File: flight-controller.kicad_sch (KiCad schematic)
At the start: 83 parts, among them J1 USB_C_Receptacle_USB2.0, J2 ESC, J3 RX, J4 GPS, J5 I2C, J6 Camera, J7 VTX, J8 DVTX, Q1 AO3400A, SW1 SW_Push, U1 AT32F435RGT7, U2 BMI270, U3 BMP280, U4 W25N01GVZEIG, U5 AT7456E, U6 TPS54302, U7 TPS54302, U8 TLV75733PDBV, U9 USBLC6-2P6, Y1 27MHz, Y2 8MHz

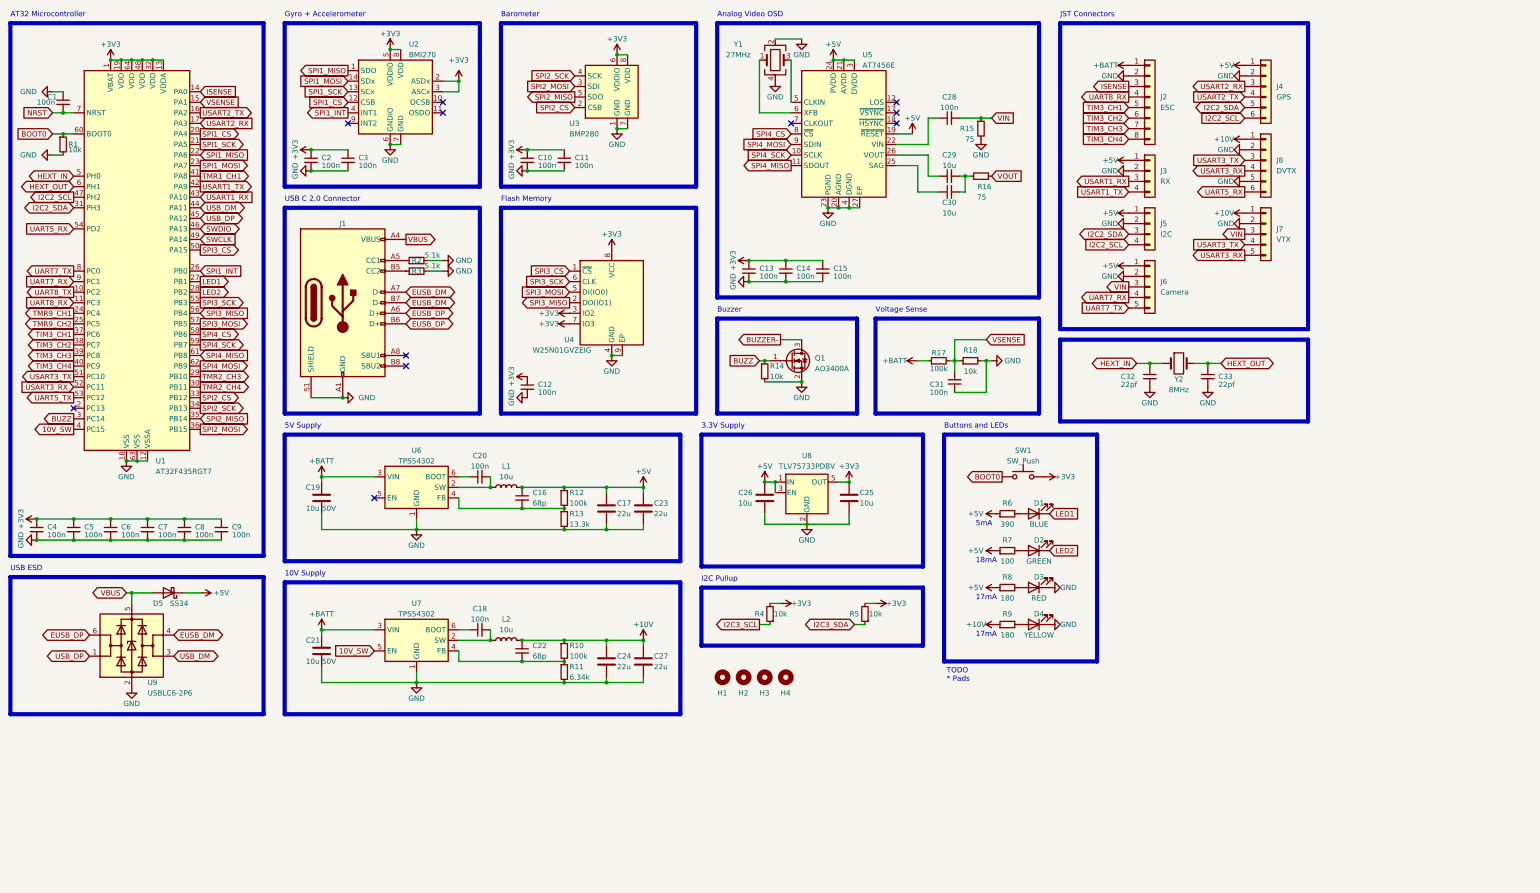
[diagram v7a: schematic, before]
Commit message: Change LED resistors to reduce current, tidy up schematic sheet, changes to AT32 pinout
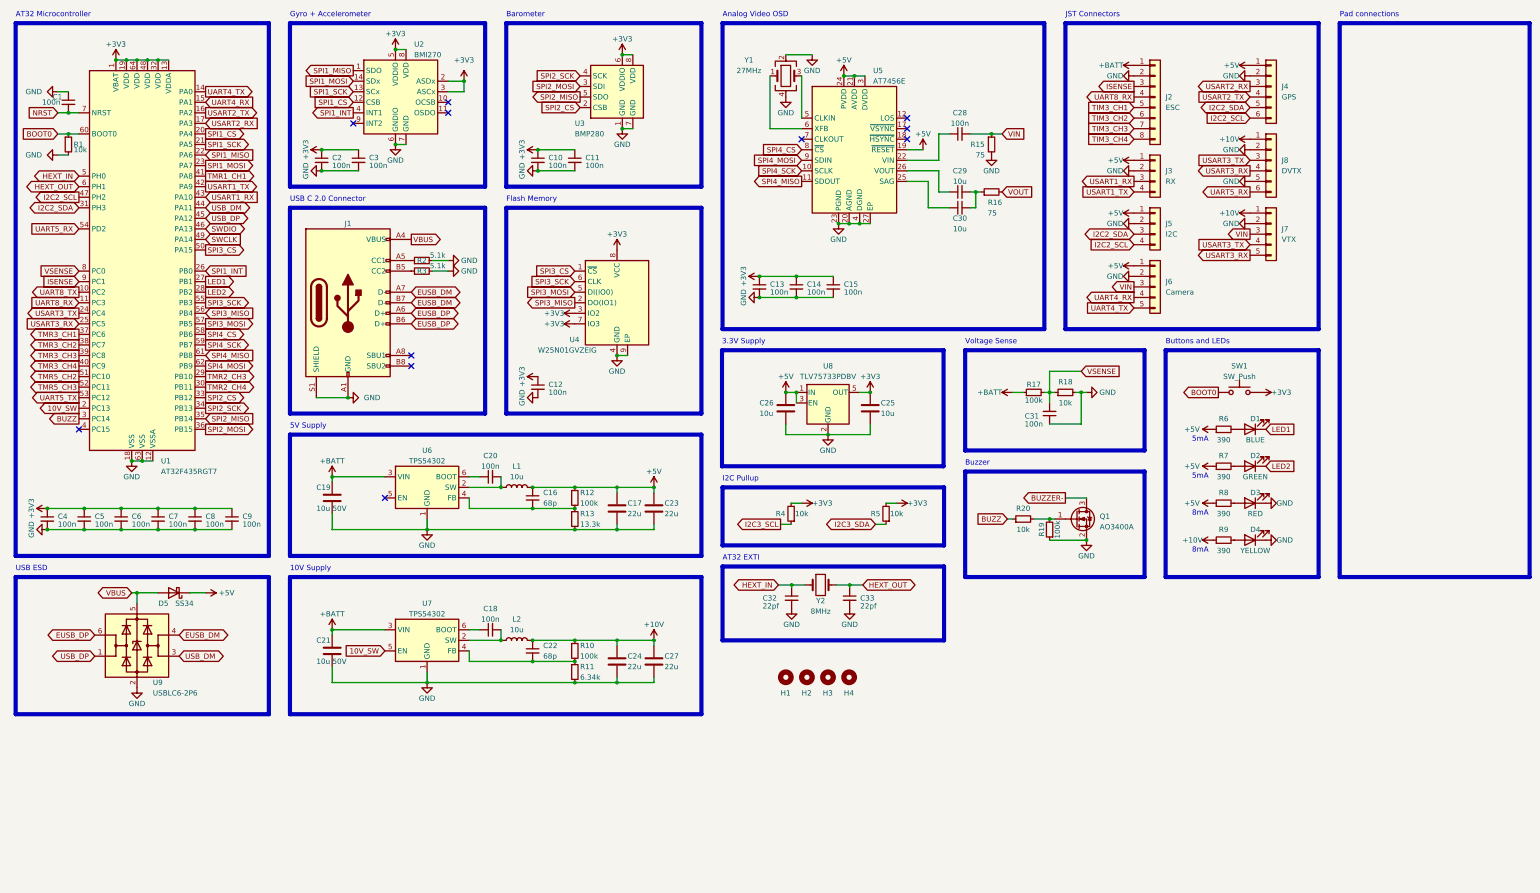
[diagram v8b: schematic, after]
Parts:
- removed R14: 10k, Resistor_SMD:R_0402_1005Metric, symbol Device:R_Small
- added R19: 100k, Resistor_SMD:R_0402_1005Metric, symbol Device:R_Small
- added R20: 10k, Resistor_SMD:R_0402_1005Metric, symbol Device:R_Small
- R6: LCSC (none) -> C23151
- R7: value 100 -> 390; LCSC C22775 -> C23151
- R8, R9: value 180 -> 390; LCSC C22828 -> C23151
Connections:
- net TMR9_CH1 is gone; now on net USART3_TX: U1.24 (PC4)
- net TMR9_CH2 is gone; now on net USART3_RX: U1.25 (PC5)
- net 10V_SW: now also U1.2 (PC13); no longer U1.4 (PC15)
- net BUZZ: now also R20.1; no longer Q1.1 (G)
- net GND: now also R19.1
- net ISENSE: now also U1.9 (PC1); no longer U1.14 (PA0)
- net TIM3_CH1: no longer U1.37 (PC6)
- net TIM3_CH2: no longer U1.38 (PC7)
- net TIM3_CH3: no longer U1.39 (PC8)
- net TIM3_CH4: no longer U1.40 (PC9)
- net USART3_RX: no longer U1.52 (PC11)
- net USART3_TX: no longer U1.51 (PC10)
- net VSENSE: now also U1.8 (PC0); no longer U1.15 (PA1)
- net UART7_RX renamed UART4_RX
- net UART4_RX: now also U1.15 (PA1); no longer U1.9 (PC1)
- net UART7_TX renamed UART4_TX
- net UART4_TX: now also U1.14 (PA0); no longer U1.8 (PC0)
- new net: Q1.1 (G), R19.2, R20.2
- new net TMR3_CH1: U1.37 (PC6)
- new net TMR3_CH2: U1.38 (PC7)
- new net TMR3_CH3: U1.39 (PC8)
- new net TMR3_CH4: U1.40 (PC9)
- new net TMR5_CH2: U1.51 (PC10)
- new net TMR5_CH3: U1.52 (PC11)
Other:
- note added: "8mA"
- note added: "AT32 EXTI"
- note added: "Pad connections"
- note removed: "17mA"
- note removed: "18mA"
- note removed: "TODO * Pads"
- moved on the sheet: C1, C10, C11, C12, C13, C14, C15, C16, C17, C18, C19, C2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
